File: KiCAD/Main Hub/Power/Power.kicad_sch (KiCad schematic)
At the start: 17 parts, among them J1 Screw_Terminal_01x02, J2 Conn_01x08_Pin, J3 Conn_01x08_Pin, J4 Conn_01x08_Pin, J5 Conn_01x08_Pin, J6 Conn_01x08_Pin, J7 Conn_01x08_Pin

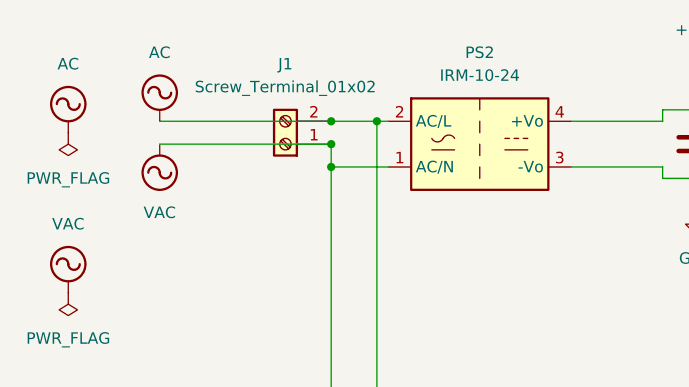
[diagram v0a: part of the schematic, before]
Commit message: Horizontal power board
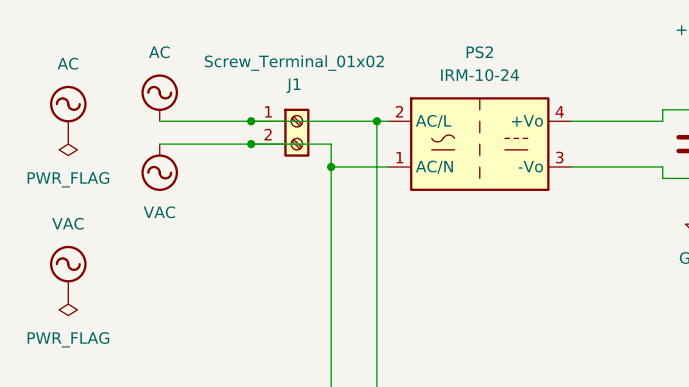
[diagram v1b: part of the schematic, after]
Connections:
- net AC: now also J1.1 (Pin_1); no longer J1.2 (Pin_2)
- net VAC: now also J1.2 (Pin_2); no longer J1.1 (Pin_1)
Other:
- moved on the sheet: J1
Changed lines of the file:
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@@
+	)
+	(junction
+		(at 49.53 30.48)
+		(diameter 0)
+		(color 0 0 0 0)
 	)
 	(junction
@@
 	)
 	(junction
-		(at 58.42 27.94)
-		(diameter 0)
-		(color 0 0 0 0)
-	)
-	(junction
 		(at 124.46 72.39)
 		(diameter 0)
@@
 	)
 	(junction
-		(at 58.42 30.48)
-		(diameter 0)
-		(color 0 0 0 0)
-	)
-	(junction
 		(at 140.97 77.47)
 		(diameter 0)
@@
 	)
 	(junction
+		(at 49.53 27.94)
+		(diameter 0)
+		(color 0 0 0 0)
+	)
+	(junction
 		(at 109.22 43.18)
 		(diameter 0)
@@
 	(wire
 		(pts
+			(xy 49.53 30.48) (xy 58.42 30.48)
+		)
+		(stroke
+			(width 0)
+			(type default)
+		)
+	)
+	(wire
+		(pts
 			(xy 58.42 33.02) (xy 64.77 33.02)
 		)
@@
 	(wire
 		(pts
+			(xy 39.37 27.94) (xy 49.53 27.94)
+		)
+		(stroke
+			(width 0)
+			(type default)
+		)
+	)
+	(wire
+		(pts
 			(xy 99.06 26.67) (xy 109.22 26.67)
 		)
@@
 	(wire
 		(pts
-			(xy 58.42 27.94) (xy 63.5 27.94)
-		)
-		(stroke
-			(width 0)
-			(type default)
-		)
-	)
-	(wire
-		(pts
 			(xy 140.97 85.09) (xy 140.97 87.63)
 		)
@@
 	(wire
 		(pts
+			(xy 49.53 27.94) (xy 63.5 27.94)
+		)
+		(stroke
+			(width 0)
+			(type default)
+		)
+	)
+	(wire
+		(pts
 			(xy 125.73 34.29) (xy 125.73 36.83)
 		)
@@
 	(wire
 		(pts
-			(xy 39.37 27.94) (xy 58.42 27.94)
-		)
-		(stroke
-			(width 0)
-			(type default)
-		)
-	)
-	(wire
-		(pts
 			(xy 158.75 69.85) (xy 158.75 72.39)
 		)
@@
 	(wire
 		(pts
-			(xy 39.37 30.48) (xy 58.42 30.48)
+			(xy 39.37 30.48) (xy 49.53 30.48)
 		)
 		(stroke
@@
 	(symbol
 		(lib_id "Connector:Screw_Terminal_01x02")
-		(at 53.34 30.48 180)
+		(at 54.61 27.94 0)
 		(unit 1)
 		(exclude_from_sim no)
@@
 		(dnp no)
 		(property "Reference" "J1"
-			(at 53.34 21.59 0)
+			(at 54.356 23.876 0)
 			(effects
 				(font
@@
 		)
 		(property "Value" "Screw_Terminal_01x02"
-			(at 53.34 24.13 0)
+			(at 54.356 21.336 0)
 			(effects
 				(font
@@
 		)
 		(property "Footprint" "TerminalBlock_Phoenix:TerminalBlock_Phoenix_MKDS-1,5-2-5.08_1x02_P5.08mm_Horizontal"
-			(at 53.34 30.48 0)
+			(at 54.61 27.94 0)
 			(effects
 				(font
@@
 		)
 		(property "Datasheet" "~"
-			(at 53.34 30.48 0)
+			(at 54.61 27.94 0)
 			(effects
 				(font
@@
 		)
 		(property "Description" "Generic screw terminal, single row, 01x02, script generated (kicad-library-utils/schlib/autogen/connector/)"
-			(at 53.34 30.48 0)
-			(effects
-				(font
+			(at 54.61 27.94 0)
+			(effects
+				(font
